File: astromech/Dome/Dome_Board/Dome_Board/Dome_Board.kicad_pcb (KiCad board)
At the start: 2 copper layers, 3 parts, among them J1 Conn_01x02_Socket, J2 Conn_01x02_Socket, U1 ESP32-C6-DEVKITC-1-N8

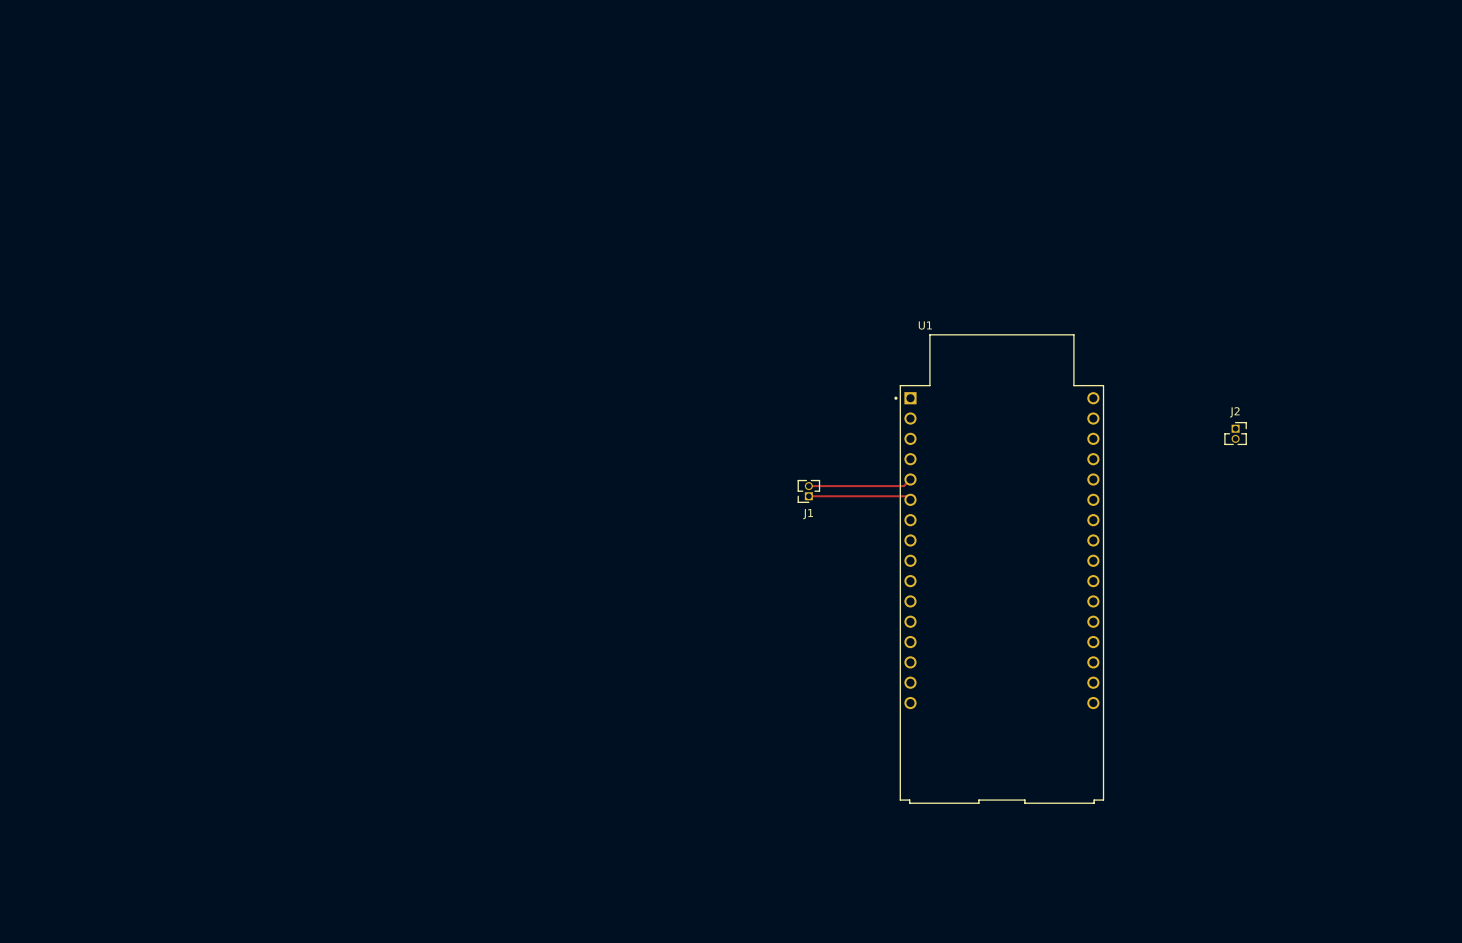
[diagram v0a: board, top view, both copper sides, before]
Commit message: added battery 5vRegulator 10/12
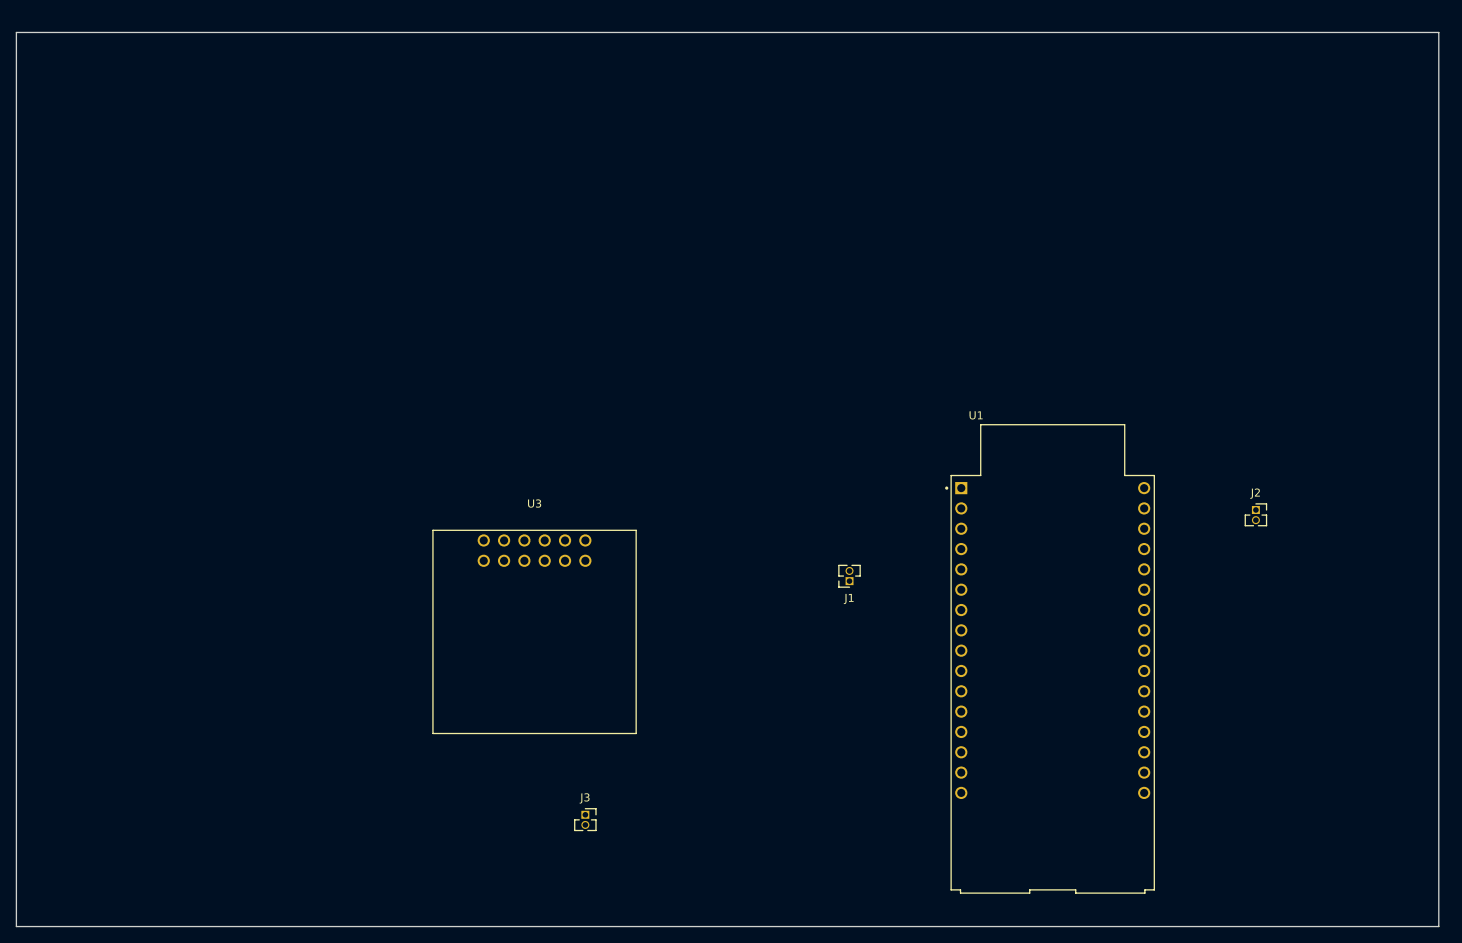
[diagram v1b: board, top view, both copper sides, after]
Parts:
- added J3: Conn_01x02_Socket, Connector_PinSocket_1.27mm:PinSocket_1x02_P1.27mm_Vertical, F.Cu at (116.8, 118.1)
- added U3: D36V50F5_Pololu, js:D36V50F5_Pololu, F.Cu at (110.5, 95.2)
- moved U1 12.9 mm to (175.3, 101.6)
- moved J1 11.8 mm to (149.9, 88.9)
- moved J2 10.5 mm to (200.7, 80.0)
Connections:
- U1 pad J1_14: unconnected-(U1-VCC_5V-PadJ1_14) -> +5V
- U1 pad J1_15: unconnected-(U1-GND_J1_15-PadJ1_15) -> GND
- U1 pad J3_1: unconnected-(U1-GND_J3_1-PadJ3_1) -> GND
- U1 pad J3_12: unconnected-(U1-GND_J3_12-PadJ3_12) -> GND
- U1 pad J3_15: unconnected-(U1-GND_J3_15-PadJ3_15) -> GND
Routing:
- net sda: track 13.0 -> 0.00 mm
- net scl: track 12.9 -> 0.00 mm
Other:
- board outline added: 177.8 x 111.8 mm

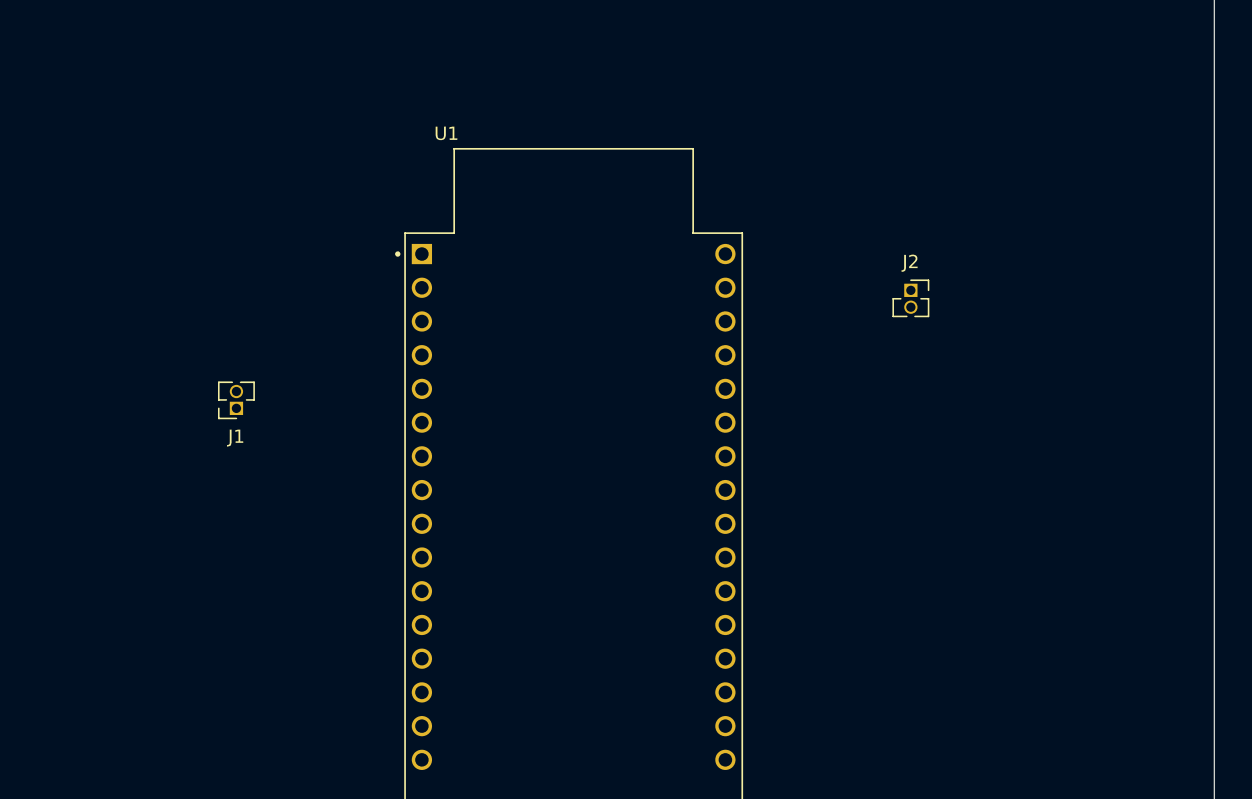
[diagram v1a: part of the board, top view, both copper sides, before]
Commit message: added txd lp, rxd lp, pwd connectors
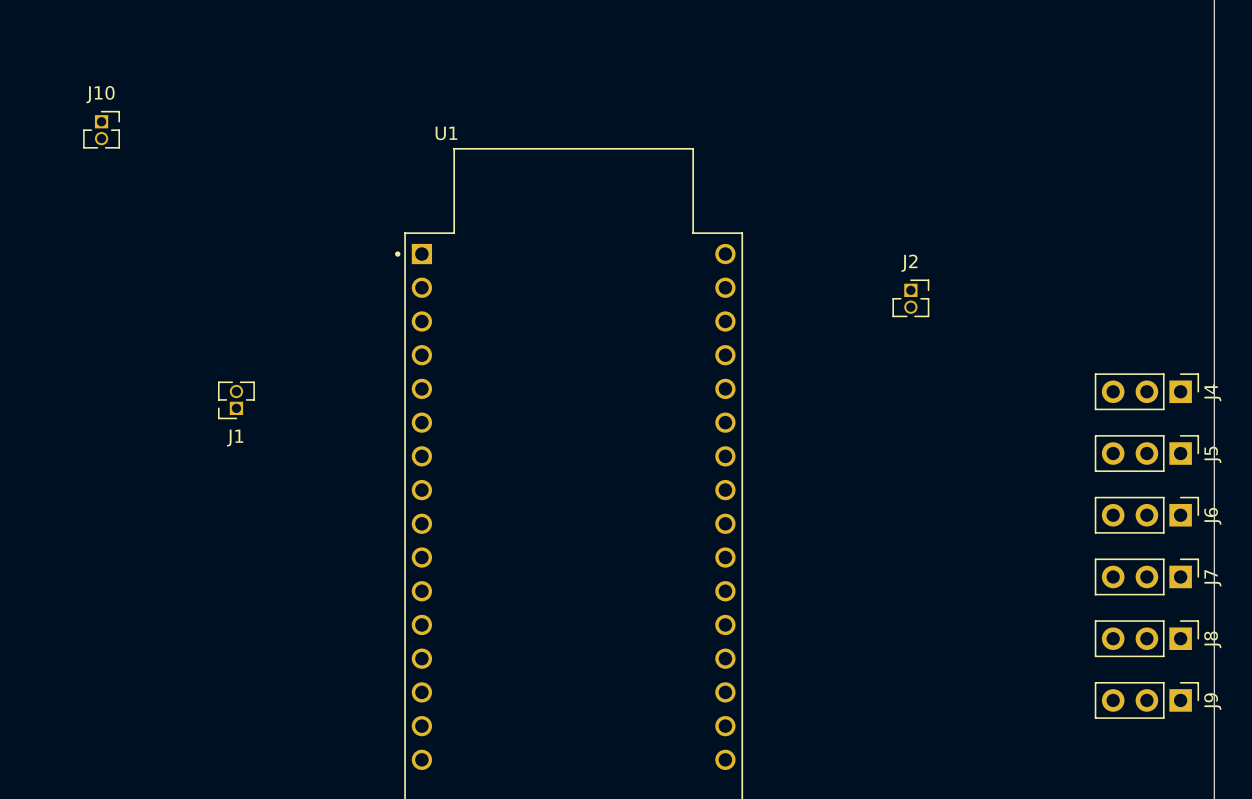
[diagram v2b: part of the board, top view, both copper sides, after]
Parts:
- added J10: Conn_01x02_Socket, Connector_PinSocket_1.27mm:PinSocket_1x02_P1.27mm_Vertical, F.Cu at (139.7, 67.3)
- added J4: Conn_01x03_Pin, Connector_PinHeader_2.54mm:PinHeader_1x03_P2.54mm_Vertical, F.Cu at (221.0, 87.7)
- added J5: Conn_01x03_Pin, Connector_PinHeader_2.54mm:PinHeader_1x03_P2.54mm_Vertical, F.Cu at (221.0, 92.3)
- added J6: Conn_01x03_Pin, Connector_PinHeader_2.54mm:PinHeader_1x03_P2.54mm_Vertical, F.Cu at (221.0, 97.0)
- added J7: Conn_01x03_Pin, Connector_PinHeader_2.54mm:PinHeader_1x03_P2.54mm_Vertical, F.Cu at (221.0, 101.6)
- added J8: Conn_01x03_Pin, Connector_PinHeader_2.54mm:PinHeader_1x03_P2.54mm_Vertical, F.Cu at (221.0, 106.2)
- added J9: Conn_01x03_Pin, Connector_PinHeader_2.54mm:PinHeader_1x03_P2.54mm_Vertical, F.Cu at (221.0, 110.9)
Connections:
- J3 pad 2: unconnected-(J3-Pin_2-Pad2) -> GND
- U1 pad J1_3: unconnected-(U1-GPIO4-PadJ1_3) -> txd lp
- U1 pad J1_4: unconnected-(U1-GPIO5-PadJ1_4) -> rxd lp
- U1 pad J3_10: unconnected-(U1-GPIO18-PadJ3_10) -> PWM 6
- U1 pad J3_5: unconnected-(U1-GPIO23-PadJ3_5) -> PWM 1
- U1 pad J3_6: unconnected-(U1-GPIO22-PadJ3_6) -> PWM 2
- U1 pad J3_7: unconnected-(U1-GPIO21-PadJ3_7) -> PWM 3
- U1 pad J3_8: unconnected-(U1-GPIO20-PadJ3_8) -> PWM 4
- U1 pad J3_9: unconnected-(U1-GPIO19-PadJ3_9) -> PWM 5

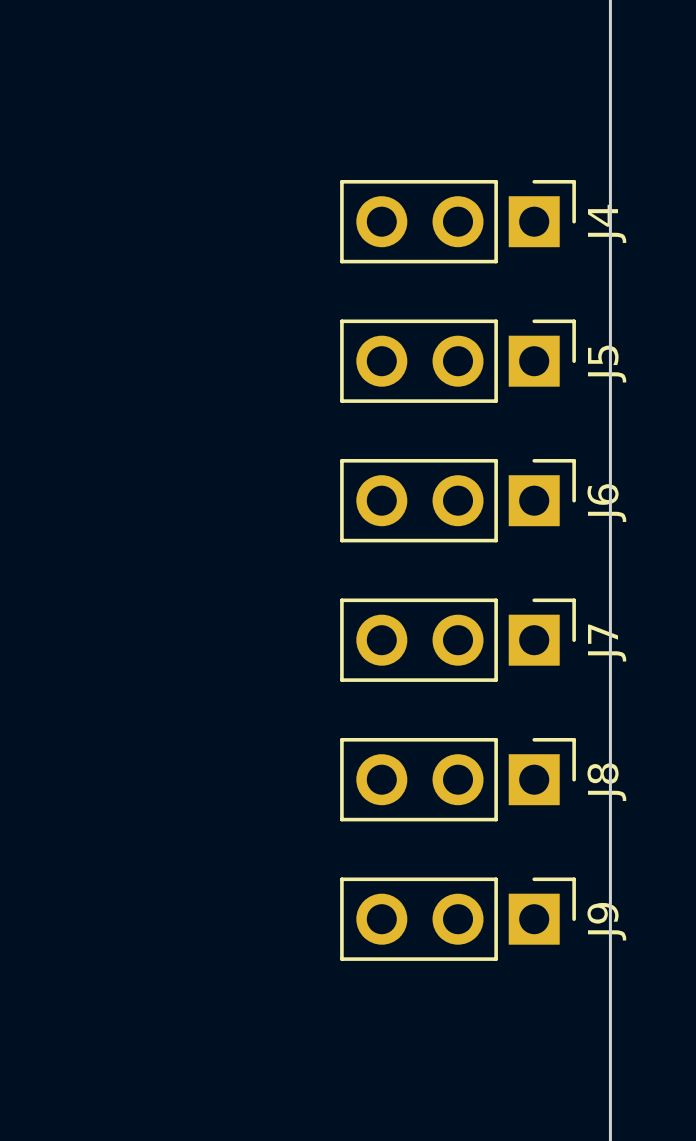
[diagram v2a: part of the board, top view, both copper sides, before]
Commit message: added txd lp, rxd lp, PWM connectors
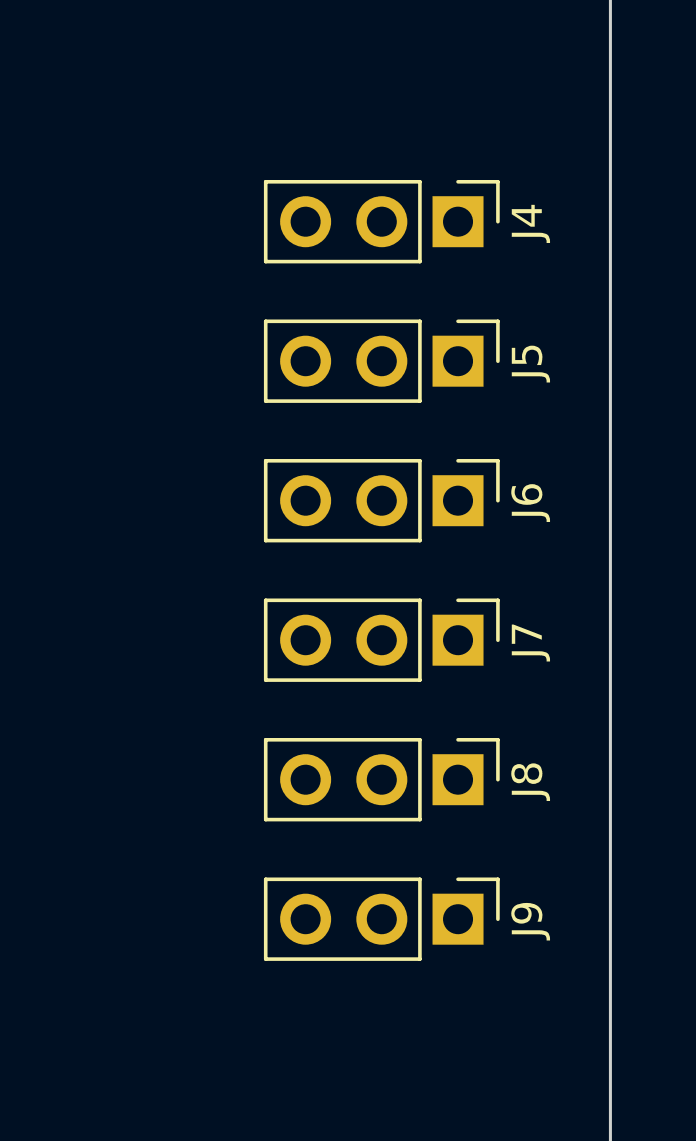
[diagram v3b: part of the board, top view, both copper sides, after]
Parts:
- moved J4 2.54 mm to (218.4, 87.7)
- moved J5 2.54 mm to (218.4, 92.3)
- moved J6 2.54 mm to (218.4, 97.0)
- moved J7 2.54 mm to (218.4, 101.6)
- moved J8 2.54 mm to (218.4, 106.2)
- moved J9 2.54 mm to (218.4, 110.9)
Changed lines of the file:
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@@
 	(footprint "Connector_PinHeader_2.54mm:PinHeader_1x03_P2.54mm_Vertical"
 		(layer "F.Cu")
-		(at 220.98 92.3 -90)
+		(at 218.44 92.3 -90)
 		(descr "Through hole straight pin header, 1x03, 2.54mm pitch, single row")
 		(tags "Through hole pin header THT 1x03 2.54mm single row")
@@
 		)
 		(fp_text user "${REFERENCE}"
-			(at 0 2.54 360)
+			(at 0 2.54 0)
 			(layer "F.Fab")
 			(effects
@@
 	(footprint "Connector_PinHeader_2.54mm:PinHeader_1x03_P2.54mm_Vertical"
 		(layer "F.Cu")
-		(at 220.98 101.6 -90)
+		(at 218.44 101.6 -90)
 		(descr "Through hole straight pin header, 1x03, 2.54mm pitch, single row")
 		(tags "Through hole pin header THT 1x03 2.54mm single row")
@@
 		)
 		(fp_text user "${REFERENCE}"
-			(at 0 2.54 360)
+			(at 0 2.54 0)
 			(layer "F.Fab")
 			(effects
@@
 	(footprint "Connector_PinHeader_2.54mm:PinHeader_1x03_P2.54mm_Vertical"
 		(layer "F.Cu")
-		(at 220.98 110.9 -90)
+		(at 218.44 110.9 -90)
 		(descr "Through hole straight pin header, 1x03, 2.54mm pitch, single row")
 		(tags "Through hole pin header THT 1x03 2.54mm single row")
@@
 		)
 		(fp_text user "${REFERENCE}"
-			(at 0 2.54 360)
+			(at 0 2.54 0)
 			(layer "F.Fab")
 			(effects
@@
 	(footprint "Connector_PinHeader_2.54mm:PinHeader_1x03_P2.54mm_Vertical"
 		(layer "F.Cu")
-		(at 220.98 87.65 -90)
+		(at 218.44 87.65 -90)
 		(descr "Through hole straight pin header, 1x03, 2.54mm pitch, single row")
 		(tags "Through hole pin header THT 1x03 2.54mm single row")
@@
 		)
 		(fp_text user "${REFERENCE}"
-			(at 0 2.54 360)
+			(at 0 2.54 0)
 			(layer "F.Fab")
 			(effects
@@
 	(footprint "Connector_PinHeader_2.54mm:PinHeader_1x03_P2.54mm_Vertical"
 		(layer "F.Cu")
-		(at 220.98 96.95 -90)
+		(at 218.44 96.95 -90)
 		(descr "Through hole straight pin header, 1x03, 2.54mm pitch, single row")
 		(tags "Through hole pin header THT 1x03 2.54mm single row")
@@
 		)
 		(fp_text user "${REFERENCE}"
-			(at 0 2.54 360)
+			(at 0 2.54 0)
 			(layer "F.Fab")
 			(effects
@@
 	(footprint "Connector_PinHeader_2.54mm:PinHeader_1x03_P2.54mm_Vertical"
 		(layer "F.Cu")
-		(at 220.98 106.25 -90)
+		(at 218.44 106.25 -90)
 		(descr "Through hole straight pin header, 1x03, 2.54mm pitch, single row")
 		(tags "Through hole pin header THT 1x03 2.54mm single row")
@@
 		)
 		(fp_text user "${REFERENCE}"
-			(at 0 2.54 360)
-			(layer "F.Fab")
-			(effects
+			(at 0 2.54 0)
+			(layer "F.Fab")
+			(effects
